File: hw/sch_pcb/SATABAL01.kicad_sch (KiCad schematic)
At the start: 7 parts, among them J1 Conn_Coaxial SMA or MCX, T1 ETC1-1-13, T2 ETC1-1-13

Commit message: PCB layout WIP.
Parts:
- added J1: SATA7-67491-1030, Mlab_CON:SATA-7_THT_VERT_2, symbol FMC2DIFF-rescue:SATA7-67491-1030-konektory
- added J2: Conn_Coaxial SMA or MCX, Connector_Coaxial:SMA_Amphenol_901-144_Vertical, symbol Connector:Conn_Coaxial
- H1, H2: footprint MountingHole:MountingHole_2.2mm_M2_Pad -> Mlab_Mechanical:MountingHole_3mm
- H3: renamed from H5; footprint MountingHole:MountingHole_2.2mm_M2_Pad -> Mlab_Mechanical:MountingHole_3mm
- H4: renamed from H6; footprint MountingHole:MountingHole_2.2mm_M2_Pad -> Mlab_Mechanical:MountingHole_3mm
- renumbered J1 to J3
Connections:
- net GND: now also J2.2 (Ext)
- net IN1: no longer T1.1 (AA), T2.1 (AA)
- net IN2: no longer T1.2 (AB), T2.5 (SB)
- net OUT renamed OUT1
- net OUT1: no longer T2.2 (AB)
- new net DGND: J1.1, J1.4, J1.7, J1.8 (4), J1.9 (7)
- new net IN1N: J1.2, T1.2 (AB)
- new net IN1P: J1.3, T1.1 (AA)
- new net IN2N: J1.5, T2.2 (AB)
- new net IN2P: J1.6, T2.1 (AA)
- new net OUT2: J2.1 (In), T2.5 (SB)

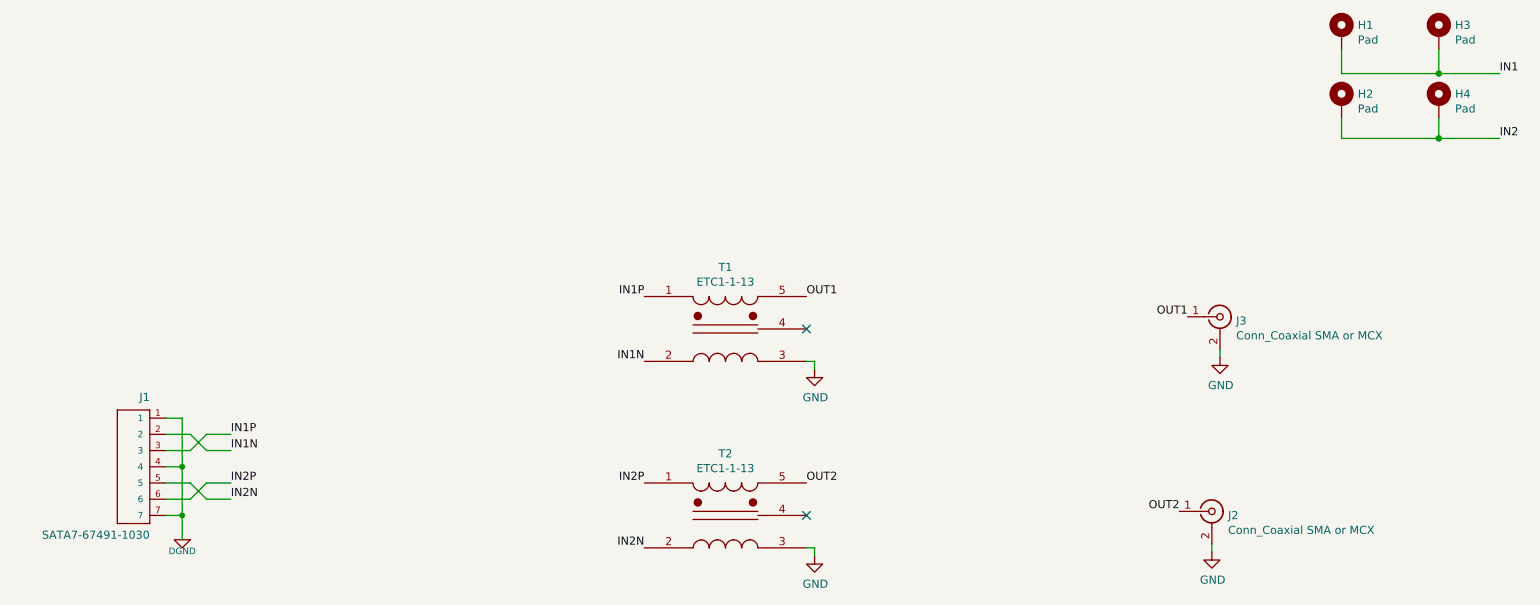
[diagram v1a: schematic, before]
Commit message: Fix issue in ground connection.
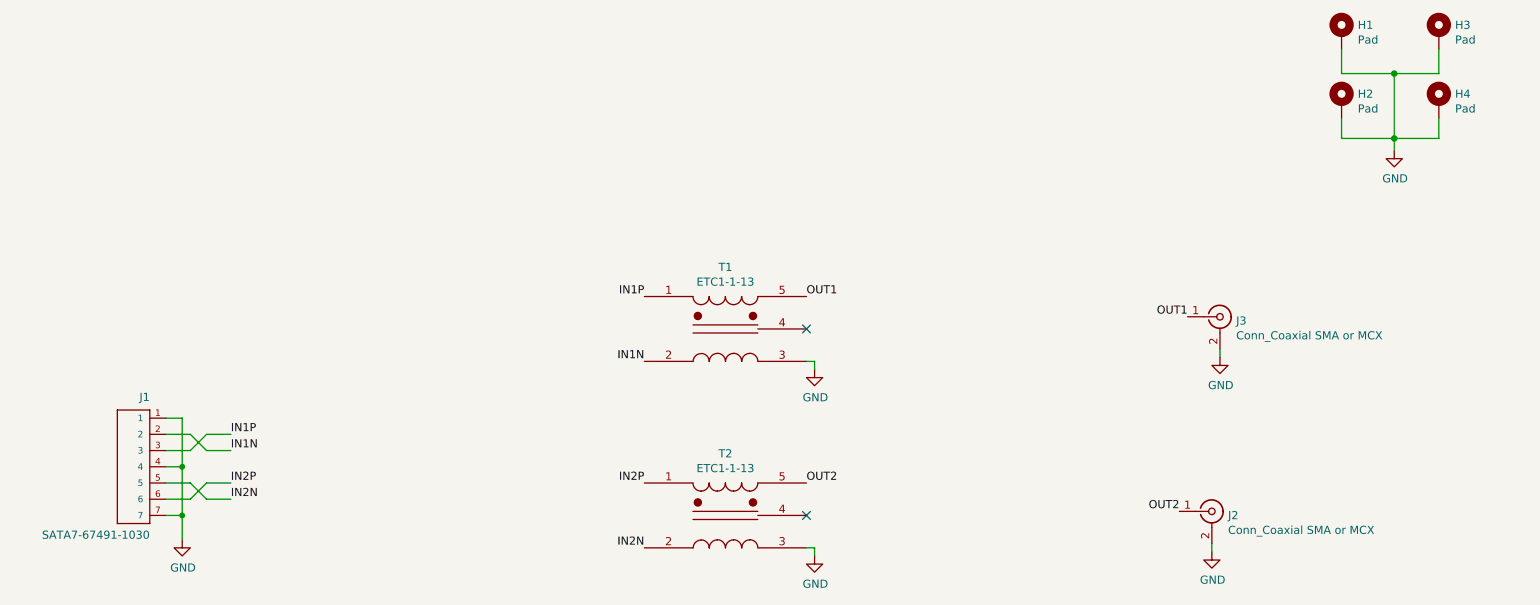
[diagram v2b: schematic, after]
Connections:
- net DGND is gone; now on net GND: J1.1, J1.4, J1.7, J1.8 (4), J1.9 (7)
- net IN1 is gone; now on net GND: H1.1, H3.1
- net IN2 is gone; now on net GND: H2.1, H4.1
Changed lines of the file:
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@@
   (junction (at 67.31 88.9) (diameter 0.9144) (color 0 0 0 0))
   (junction (at 67.31 96.52) (diameter 0.9144) (color 0 0 0 0))
-  (junction (at 264.16 27.305) (diameter 1.016) (color 0 0 0 0))
-  (junction (at 264.16 37.465) (diameter 1.016) (color 0 0 0 0))
+  (junction (at 257.175 27.305) (diameter 1.016) (color 0 0 0 0))
+  (junction (at 257.175 37.465) (diameter 1.016) (color 0 0 0 0))
   (no_connect (at 165.1 67.31))
   (no_connect (at 165.1 96.52))
@@
     (stroke (width 0) (type solid) (color 0 0 0 0))
   )
-  (wire (pts (xy 248.92 27.305) (xy 264.16 27.305))
+  (wire (pts (xy 248.92 27.305) (xy 257.175 27.305))
     (stroke (width 0) (type solid) (color 0 0 0 0))
   )
@@
     (stroke (width 0) (type solid) (color 0 0 0 0))
   )
-  (wire (pts (xy 248.92 37.465) (xy 264.16 37.465))
+  (wire (pts (xy 248.92 37.465) (xy 257.175 37.465))
+    (stroke (width 0) (type solid) (color 0 0 0 0))
+  )
+  (wire (pts (xy 257.175 27.305) (xy 257.175 37.465))
+    (stroke (width 0) (type solid) (color 0 0 0 0))
+  )
+  (wire (pts (xy 257.175 27.305) (xy 264.16 27.305))
+    (stroke (width 0) (type solid) (color 0 0 0 0))
+  )
+  (wire (pts (xy 257.175 37.465) (xy 257.175 39.37))
+    (stroke (width 0) (type solid) (color 0 0 0 0))
+  )
+  (wire (pts (xy 257.175 37.465) (xy 264.16 37.465))
     (stroke (width 0) (type solid) (color 0 0 0 0))
   )
@@
     (stroke (width 0) (type solid) (color 0 0 0 0))
   )
-  (wire (pts (xy 264.16 27.305) (xy 273.685 27.305))
-    (stroke (width 0) (type solid) (color 0 0 0 0))
-  )
   (wire (pts (xy 264.16 37.465) (xy 264.16 34.29))
     (stroke (width 0) (type solid) (color 0 0 0 0))
   )
-  (wire (pts (xy 264.16 37.465) (xy 273.685 37.465))
-    (stroke (width 0) (type solid) (color 0 0 0 0))
-  )
   (label "IN1P" (at 74.93 83.82 0)
     (effects (font (size 1.27 1.27)) (justify left bottom))
@@
     (effects (font (size 1.27 1.27)) (justify right bottom))
   )
-  (label "IN1" (at 273.685 27.305 0)
-    (effects (font (size 1.27 1.27)) (justify left bottom))
-  )
-  (label "IN2" (at 273.685 37.465 0)
-    (effects (font (size 1.27 1.27)) (justify left bottom))
-  )
-  (symbol (lib_id "FMC2DIFF-rescue:DGND-RESCUE-FMC2DIFF-FMC2DIFF-rescue") (at 67.31 100.33 0) (mirror y) (unit 1)
-    (in_bom yes) (on_board yes)
-    (property "Reference" "#PWR01" (id 0) (at 67.31 100.33 0)
-      (effects (font (size 1.016 1.016)) hide)
-    )
-    (property "Value" "DGND" (id 1) (at 67.31 102.108 0)
-      (effects (font (size 1.016 1.016)))
-    )
+  (symbol (lib_id "power:GND") (at 67.31 100.33 0) (unit 1)
+    (in_bom yes) (on_board yes)
+    (property "Reference" "#PWR?" (id 0) (at 67.31 106.68 0)
+      (effects (font (size 1.27 1.27)) hide)
+    )
+    (property "Value" "GND" (id 1) (at 67.437 104.7242 0))
     (property "Footprint" "" (id 2) (at 67.31 100.33 0)
-      (effects (font (size 1.524 1.524)))
+      (effects (font (size 1.27 1.27)) hide)
     )
     (property "Datasheet" "" (id 3) (at 67.31 100.33 0)
-      (effects (font (size 1.524 1.524)))
+      (effects (font (size 1.27 1.27)) hide)
     )
     (pin "1")
@@
     )
     (property "Datasheet" "" (id 3) (at 229.87 71.755 0)
+      (effects (font (size 1.27 1.27)) hide)
+    )
+    (pin "1")
+  )
+  (symbol (lib_id "power:GND") (at 257.175 39.37 0) (unit 1)
+    (in_bom yes) (on_board yes)
+    (property "Reference" "#PWR?" (id 0) (at 257.175 45.72 0)
+      (effects (font (size 1.27 1.27)) hide)
+    )
+    (property "Value" "GND" (id 1) (at 257.302 43.7642 0))
+    (property "Footprint" "" (id 2) (at 257.175 39.37 0)
+      (effects (font (size 1.27 1.27)) hide)
+    )
+    (property "Datasheet" "" (id 3) (at 257.175 39.37 0)
       (effects (font (size 1.27 1.27)) hide)
     )
@@
   )
   (symbol_instances
-    (path "/e6b16b3d-9406-44b8-8160-d1752b2b6396"
-      (reference "#PWR01") (unit 1) (value "DGND") (footprint "")
-    )
     (path "/00000000-0000-0000-0000-00005f968856"
       (reference "#PWR02") (unit 1) (value "GND") (footprint "")
@@
       (reference "#PWR05") (unit 1) (value "GND") (footprint "")
     )
+    (path "/0a76fcc7-09db-43cd-be7a-09c3a3a66e77"
+      (reference "#PWR?") (unit 1) (value "GND") (footprint "")
+    )
+    (path "/c36adbf7-8d84-4010-94dc-90065364e7b3"
+      (reference "#PWR?") (unit 1) (value "GND") (footprint "")
+    )
     (path "/00000000-0000-0000-0000-00005f8dc398"
